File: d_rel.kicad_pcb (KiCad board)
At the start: 2 copper layers, 2 parts, among them SW1 Switch

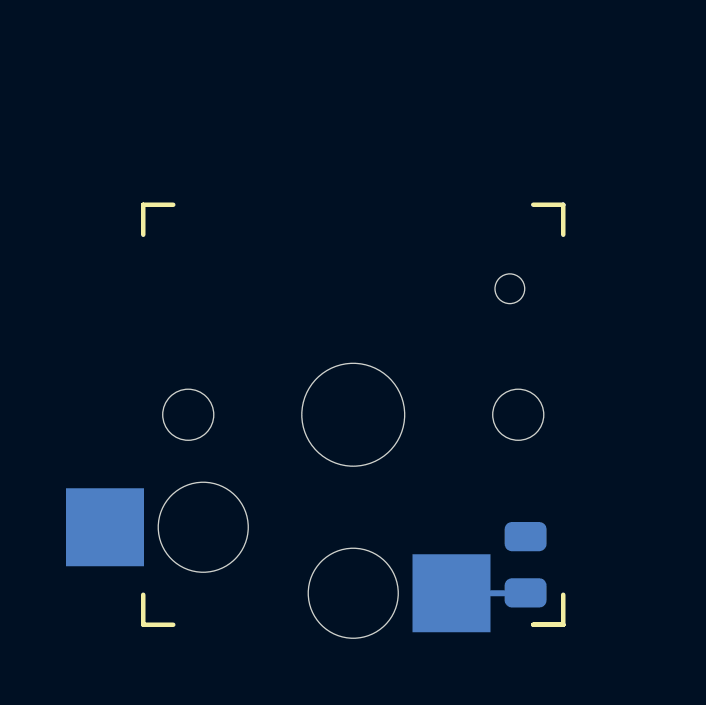
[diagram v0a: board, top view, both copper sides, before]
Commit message: making kb reversible
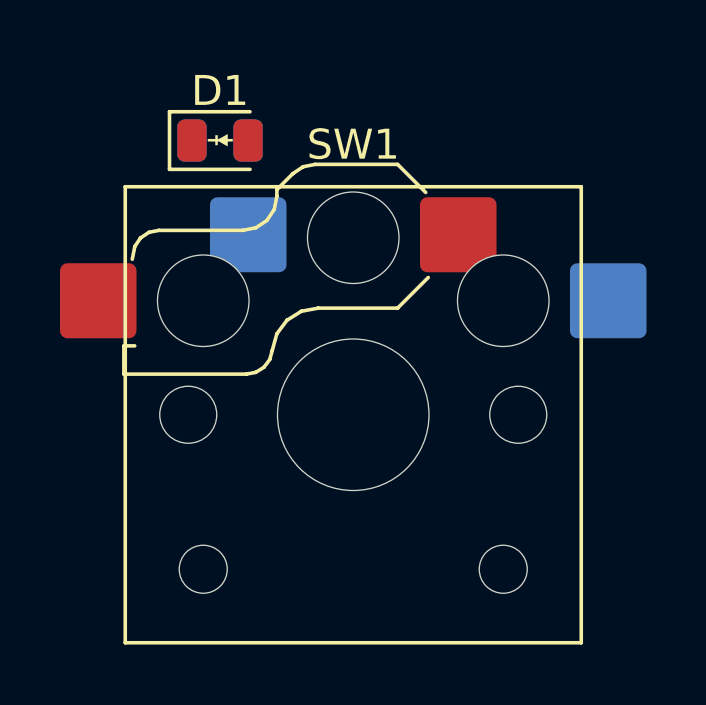
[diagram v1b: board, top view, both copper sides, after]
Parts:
- D1: footprint Diode_SMD:D_0805_2012Metric -> custom_parts:D_0805_2012Metric-Reversible; moved to F.Cu
- SW1: footprint keyswitches:Kailh_socket_PG1350 -> custom_parts:SW_Hotswap_Kailh_Choc_V1V2-Reversible
- moved D1 17.4 mm to (-4.44, -9.14), turned to 0 degrees
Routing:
- net Net-(D1-A): track 2.48 -> 0.00 mm
